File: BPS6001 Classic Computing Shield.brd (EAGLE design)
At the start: 119.4 x 58.7 mm, 85 parts, among them IC1 MAX3232CSE, X1 VGA

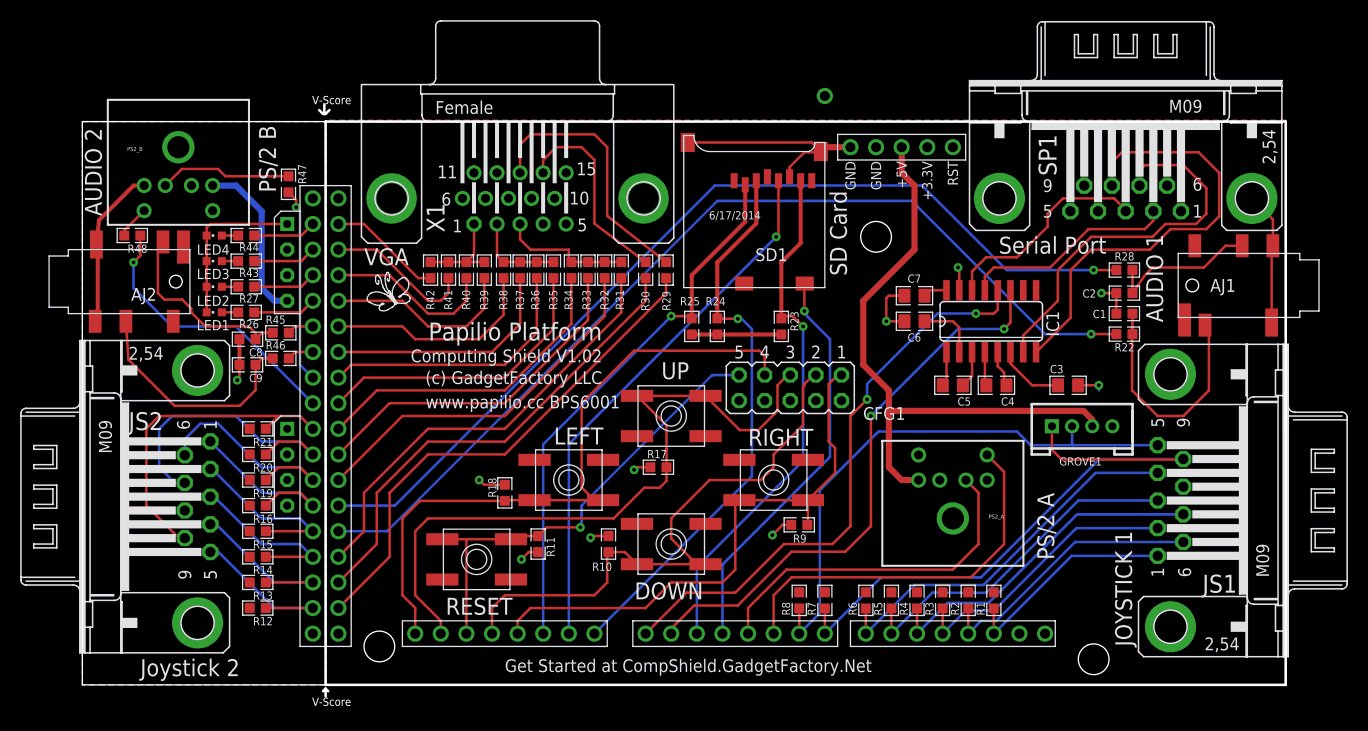
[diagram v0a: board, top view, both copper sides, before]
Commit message: First outline of design moved to Eagle 9.
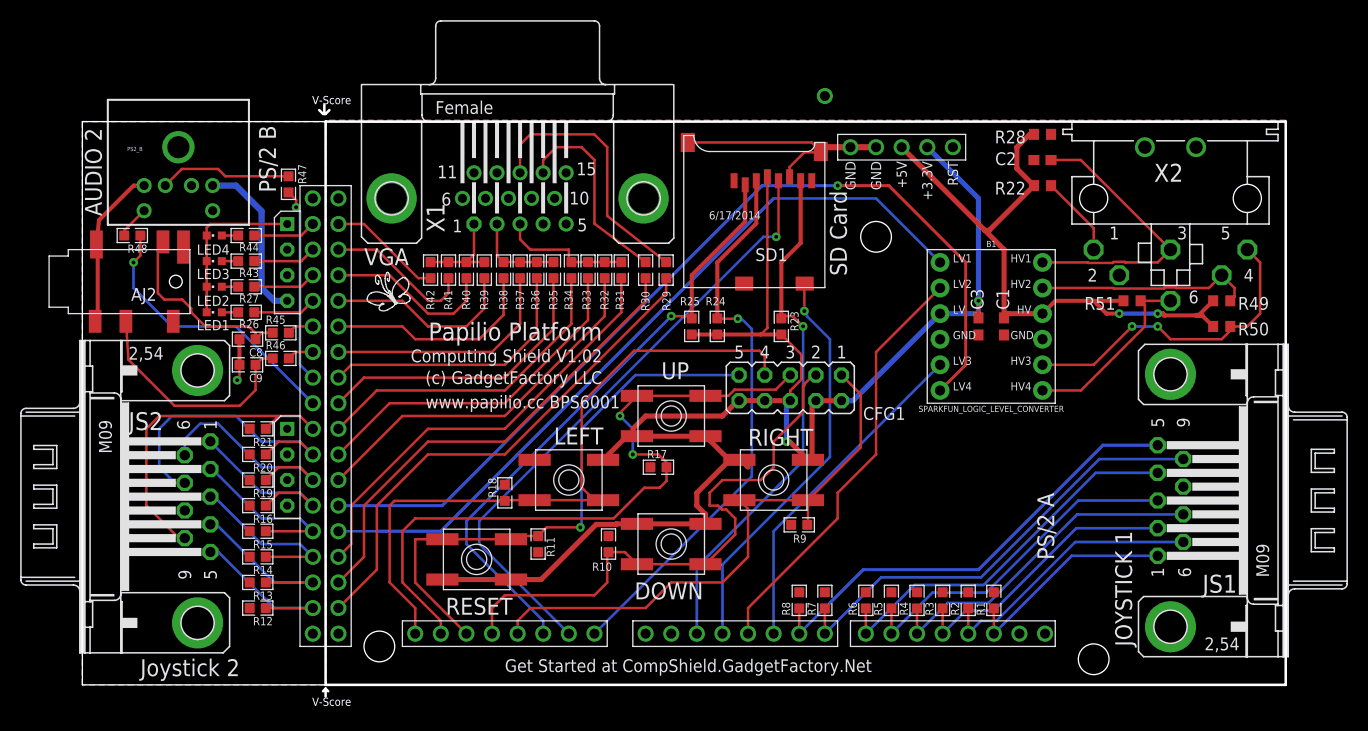
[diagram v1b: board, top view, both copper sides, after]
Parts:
- removed AJ1: AUDIO-CONNECTOR-6P-SMD-3440030P1, OPL Eagle Library:6P-SMD-3.5
- removed C4, C5, C6, C7: .1uF, GadgetFactory_6.0:0805
- removed GROVE1: (no value), GadgetFactory_6.0:CONNECTOR_4P-LEADED-2.0
- removed IC1: MAX3232CSE, maxim:SO16
- removed PS2_A: MINI-DIN6PTH, SparkFun-Connectors:MINI-DIN6
- removed SP1: Serial Port, con-subd:M09HP
- added B1: SPARKFUN_LOGIC_LEVEL_CONVERTER, SparkFun-Boards:SPARKFUN_LOGIC_LEVEL_CONVERTER
- added R49, R50, R51: 1k, resistor:R0603
- added X2: MAB6H, con-hirschmann:MAB6H
- C1, C2: value 4700pF -> 10p; device GadgetFactory:0603 -> resistor:C0603
- C3: value .1uF -> 10p; device GadgetFactory_6.0:0805 -> resistor:C0603
- R22, R28: value 3.3K -> 1k; device GadgetFactory:0603 -> resistor:R0603
- moved R22 16.8 mm to (95.2, 49.5)
- moved R28 15.7 mm to (95.2, 54.6)
- moved C2 15.5 mm to (95.2, 52.1), turned to 0 degrees
- moved C1 12.0 mm to (91.4, 35.6), turned to 270 degrees
- moved C3 10.6 mm to (88.9, 35.6), turned to 90 degrees
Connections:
- removed net 3V3: C7.1, CFG1.10, CFG1.2, CFG1.4, CFG1.6, CFG1.8, H1.3.3V, IC1.16, R1.2, R2.2, R23.2, R24.2, R25.2, R3.2, R4.2, R5.2, R6.2, R7.2, R8.2, S1.B', S2.B', S3.B', S4.B', S5.B', SD1.4
- removed net AUDIO1-LEFT: H1.D28, R22.2
- removed net AUDIO1-RIGHT: H1.D30, R28.2
- removed net CTS: IC1.9
- removed net DTE_CTS: IC1.8, SP1.8
- removed net DTE_RTS: IC1.7, SP1.7
- removed net DTE_RX: IC1.13, SP1.2
- removed net DTE_TX: IC1.14, SP1.3
- removed net N$12: C4.2, IC1.4
- removed net N$13: C5.1, IC1.3
- removed net N$14: C4.1, IC1.5
- removed net N$2: AJ1.L, C1.1, R22.1
- removed net N$34: AJ1.R, C2.1, R28.1
- removed net N$6: C6.1, IC1.2
- removed net N$7: C3.1, IC1.6
- removed net N$8: C5.2, IC1.1
- removed net PS2CLK1: H1.D5, PS2_A.5
- removed net PS2DAT1: H1.D4, PS2_A.1
- removed net RTS: IC1.10
- new net 3V3_PWR6: B1.LV, C3.2, CFG1.10, CFG1.2, CFG1.4, CFG1.6, CFG1.8, H1.3.3V, R1.2, R2.2, R23.2, R24.2, R25.2, R3.2, R4.2, R5.2, R6.2, R7.2, R8.2, S1.B, S1.B', S2.B, S2.B', S3.B, S3.B', S4.B, S4.B', S5.B', SD1.4
- new net 3V3_PWR7: PWR_2.P3
- new net IEC-H-ATN: B1.HV1, C2.2, R28.1, X2.3
- new net IEC-H-CLK: B1.HV2, R49.1, X2.4
- new net IEC-H-DATA: B1.HV3, R50.1, X2.5
- new net IEC-H-RESET: B1.HV4, R51.1, X2.6
- new net IEC-H-SRQ: R22.1, X2.1
- new net IEC-L-ATN: B1.LV1, H1.D28
- new net IEC-L-CLK: B1.LV2, H1.D4
- new net IEC-L-DATA: B1.LV3, H1.D5
- new net IEC-L-RESET: B1.LV4, H1.D30
- net 5V0: now also B1.HV, C1.1, R22.2, R28.2, R49.2, R50.2, R51.2; no longer GROVE1.3, PS2_A.4
- net GND: now also B1.GND1, B1.GND2, C2.1, C3.1, X2.2, X2.PE, X2.PE@; no longer AJ1.COM1, AJ1.COM2, C2.2, C3.2, C6.2, C7.2, GROVE1.4, IC1.15, PS2_A.3, SP1.5, SP1.G1, SP1.G2
- net JS1_5: no longer GROVE1.2
- net JS1_9: no longer GROVE1.1
- net RX: no longer IC1.12
- net TX: no longer IC1.11
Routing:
- net 3V3_PWR6: track 0.00 -> 156.4 mm, vias 0 -> 2
- net AUDIO1-LEFT: track 96.2 -> 0.00 mm, vias 1 -> 0
- net AUDIO1-RIGHT: track 93.8 -> 0.00 mm, vias 1 -> 0
- net IEC-L-RESET: track 0.00 -> 92.3 mm, vias 0 -> 1
- net IEC-L-ATN: track 0.00 -> 77.0 mm
- net RX: track 57.5 -> 0.00 mm, vias 2 -> 0
- net TX: track 56.3 -> 0.00 mm, vias 2 -> 0
- net DTE_CTS: track 45.0 -> 0.00 mm
- net IEC-L-CLK: track 0.00 -> 42.2 mm
- net DTE_RTS: track 38.5 -> 0.00 mm
- net PS2CLK1: track 38.3 -> 0.00 mm
- net GND: track 61.4 -> 23.9 mm, vias 9 -> 0
- net PS2DAT1: track 34.9 -> 0.00 mm
- net IEC-L-DATA: track 0.00 -> 33.5 mm
- net IEC-H-DATA: track 0.00 -> 32.0 mm, vias 0 -> 2
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- added copper zone on layer 1, net 3V3_PWR6
- removed copper zone on layer 1, net 3V3
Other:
- board text removed: "AUDIO 1"
- board text removed: "Serial Port"

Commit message: Fixed some issues, board is now without problems.
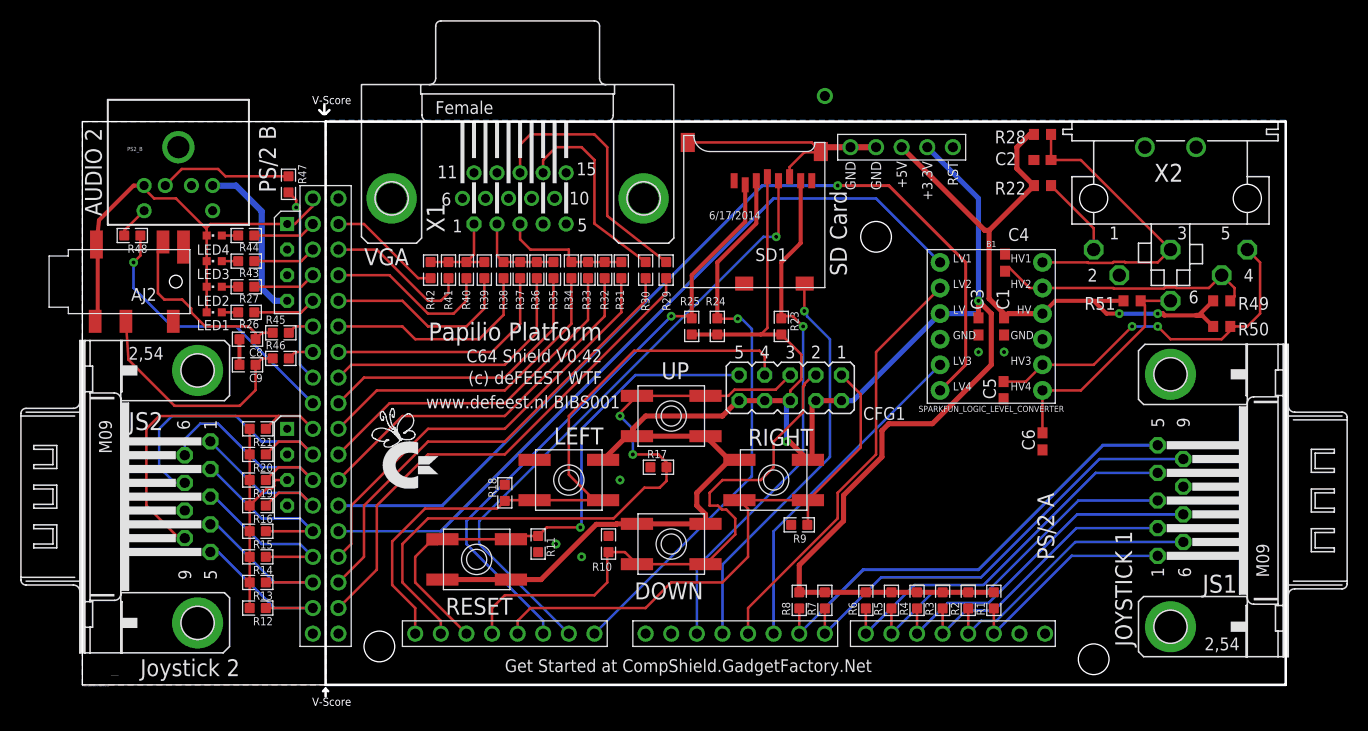
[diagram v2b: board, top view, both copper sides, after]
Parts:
- added C4, C5, C6: 10p, resistor:C0603
- moved LOGO1 13.5 mm to (31.0, 25.0)
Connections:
- net GND: now also C4.1, C5.1, C6.1
- net IEC-H-CLK: now also C4.2
- net IEC-H-DATA: now also C5.2
- net IEC-H-RESET: now also C6.2
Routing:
- net 3V3_PWR6: track 156.4 -> 215.7 mm
- net JOY_3V3: track 0.00 -> 22.8 mm
- net JOY_GND: track 37.1 -> 47.9 mm, vias 1 -> 0
- net IEC-H-CLK: track 21.6 -> 26.3 mm
- net IEC-H-DATA: track 32.0 -> 36.6 mm
- net IEC-H-RESET: track 18.5 -> 22.7 mm
- net IEC-H-ATN: track 28.8 -> 31.4 mm
- net SW_RIGHT: track 67.7 -> 66.3 mm
- net RESET: track 56.0 -> 55.0 mm
- net SW_DOWN: track 68.9 -> 67.9 mm
- net IEC-L-ATN: track 77.0 -> 76.0 mm
- net GND: vias 0 -> 5
- added copper zone on layer 1, net GND
- added copper zone on layer 1, net JOY_GND
- removed copper zone on layer 1, net 3V3_PWR6
- removed copper zone on layer 1, net JOY_3V3
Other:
- board text added: "(c) deFEEST WTF"
- board text added: "/home/paul/work/fpga/papilio/computing-shield/c64-wing/255px-CBM_Logo.svg.bmp"
- board text added: "C64 Shield V0.42"
- board text added: "www.defeest.nl BIBS001"
- board text removed: "(c) GadgetFactory LLC"
- board text removed: "Computing Shield V1.02"
- board text removed: "www.papilio.cc BPS6001"
